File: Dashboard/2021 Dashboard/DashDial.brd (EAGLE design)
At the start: 88.9 x 66.3 mm, 30 parts, among them IC2 TLC5952DAP, J1 ESW-104-23-L-D, J2 ESW-104-23-L-D

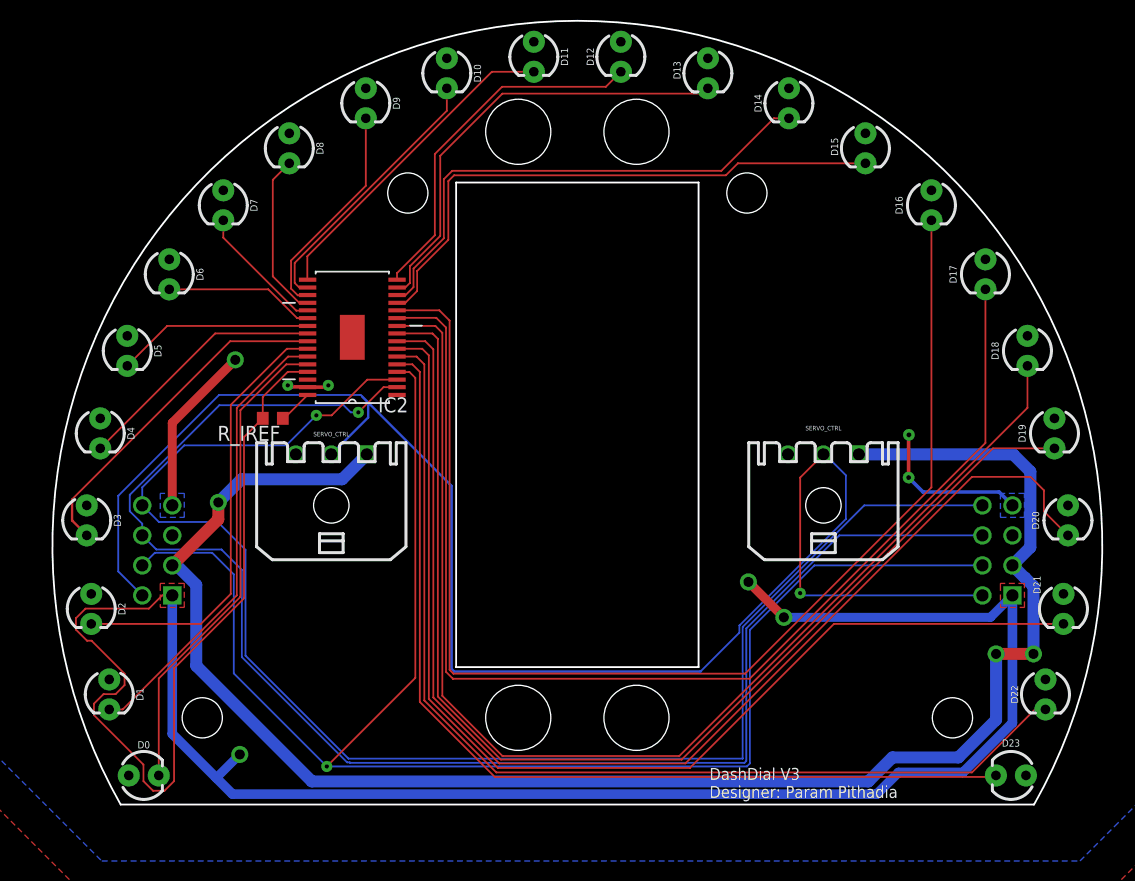
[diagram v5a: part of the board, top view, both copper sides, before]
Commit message: Updated all dashboard stuff
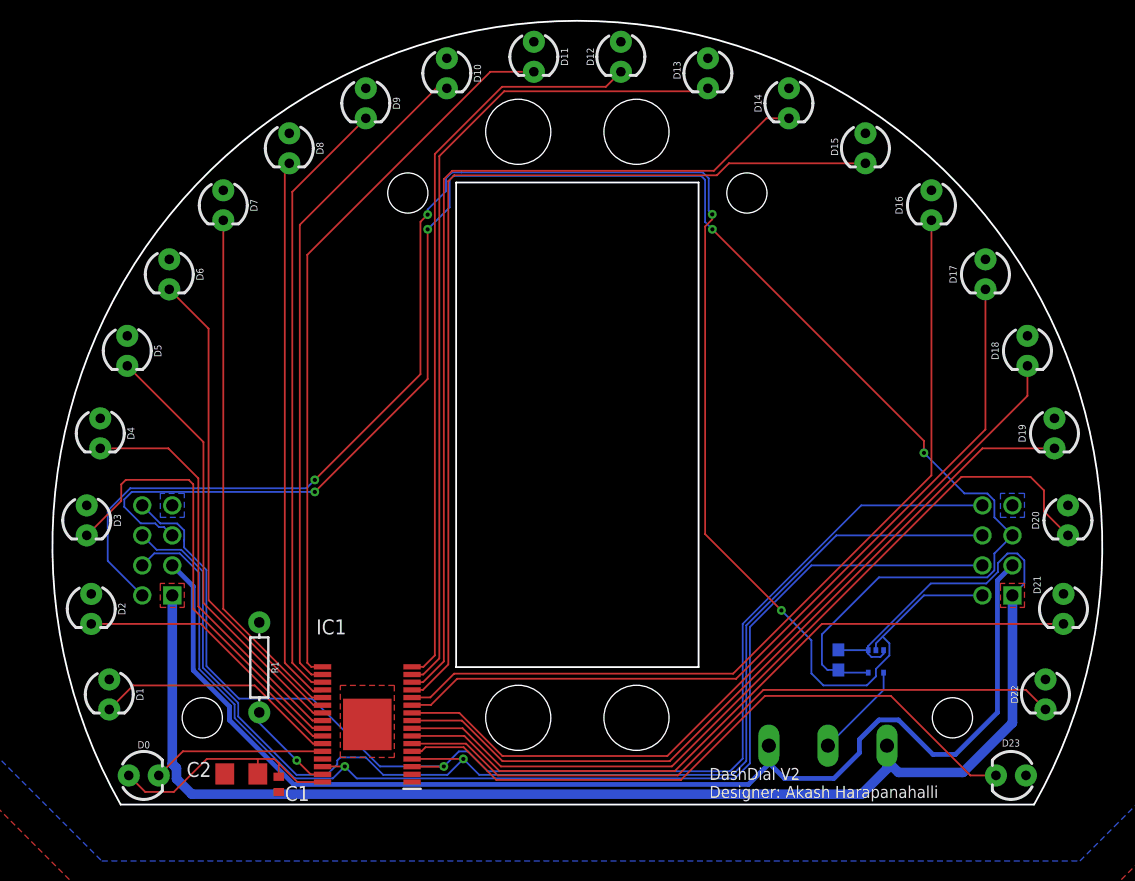
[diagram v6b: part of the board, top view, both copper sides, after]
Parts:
- removed IC2: TLC5952DAP, GTOR - Active Components:SOP65P810X120-33N
- removed R_IREF: 2.4k, GTOR - Passive Components:R0603
- removed SERVO, SERVO1: (no value), GTOR - Microfit Connector:43650-0300
- added C1: 0.1uF, rcl:C0402
- added C2: 100uF, rcl:C1206
- added C3: 0.1uF, SparkFun-Capacitors:0603
- added IC1: TLC5947DAPR, TLC5947DAPR:SOP65P810X120-33N
- added R1: 3k, SparkFun-Resistors:AXIAL-0.3
- added U1: LOGIC SHIFTER, MC74VHC1GT125:SOT353
- added X2: SERVO, con-wago-500:W237-103
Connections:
- removed net N$31: IC2.32, R_IREF.1
- new net 5V: C3.1, J1.05, J2.05, U1.5
- new net N$1: U1.4, X2.2
- new net N$32: IC1.31, R1.P$2
- net 3.3V: now also C1.2, C2.2, IC1.32; no longer IC2.31
- net 7.4V: now also X2.3; no longer SERVO.P$1, SERVO1.P$1
- net GND: now also C1.1, C2.1, C3.2, IC1.1, IC1.2, IC1.33, R1.P$1, U1.1, U1.3, X2.1; no longer IC2.1, IC2.29, IC2.33, R_IREF.2, SERVO.P$3, SERVO1.P$3
- net LAT: now also IC1.30; no longer IC2.4
- net OUT0: now also IC1.5; no longer IC2.5
- net OUT1: now also IC1.6; no longer IC2.6
- net OUT10: now also IC1.15; no longer IC2.15
- net OUT11: now also IC1.16; no longer IC2.16
- net OUT12: now also IC1.17; no longer IC2.17
- net OUT13: now also IC1.18; no longer IC2.18
- net OUT14: now also IC1.19; no longer IC2.19
- net OUT15: now also IC1.20; no longer IC2.20
- net OUT16: now also IC1.21; no longer IC2.21
- net OUT17: now also IC1.22; no longer IC2.22
- net OUT18: now also IC1.23; no longer IC2.23
- net OUT19: now also IC1.24; no longer IC2.24
- net OUT2: now also IC1.7; no longer IC2.7
- net OUT20: now also IC1.25; no longer IC2.25
- net OUT21: now also IC1.26; no longer IC2.26
- net OUT22: now also IC1.27; no longer IC2.27
- net OUT23: now also IC1.28; no longer IC2.28
- net OUT3: now also IC1.8; no longer IC2.8
- net OUT4: now also IC1.9; no longer IC2.9
- net OUT5: now also IC1.10; no longer IC2.10
- net OUT6: now also IC1.11; no longer IC2.11
- net OUT7: now also IC1.12; no longer IC2.12
- net OUT8: now also IC1.13; no longer IC2.13
- net OUT9: now also IC1.14; no longer IC2.14
- net SCLK: now also IC1.3; no longer IC2.3
- net SERVO_CTRL: now also U1.2; no longer SERVO.P$2, SERVO1.P$2
- net SIN: now also IC1.4; no longer IC2.2
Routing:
- net 5V: track 0.00 -> 144.3 mm, vias 0 -> 4
- net GND: track 197.1 -> 129.6 mm, vias 3 -> 0
- net 7.4V: track 145.4 -> 103.5 mm, vias 3 -> 0
- net OUT12: track 27.6 -> 61.6 mm
- net OUT13: track 23.1 -> 56.7 mm
- net LAT: track 135.4 -> 101.8 mm
- net OUT5: track 102.2 -> 68.8 mm
- net OUT14: track 18.7 -> 51.9 mm
- net OUT16: track 11.2 -> 44.4 mm
- net OUT11: track 30.6 -> 63.4 mm
- net OUT15: track 14.0 -> 46.7 mm
- net OUT4: track 99.2 -> 66.8 mm
- net OUT10: track 38.1 -> 70.5 mm
- net OUT8: track 48.4 -> 80.8 mm
- net OUT9: track 43.2 -> 75.6 mm
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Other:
- board text added: "DashDial V2 Designer: Akash Harapanahalli"
- board text removed: "DashDial V3 Designer: Param Pithadia"
- board text removed: "SERVO_CTRL"
